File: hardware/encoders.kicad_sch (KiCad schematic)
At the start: 19 parts

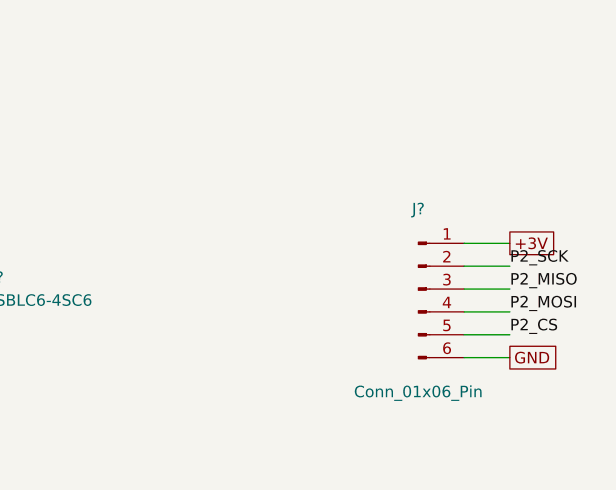
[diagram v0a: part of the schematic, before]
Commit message: Add sensing sheet; update MCU, CAN FD, encoder and root schematics
Co-Authored-By: Claude Opus 5.5 <noreply@anthropic.com>
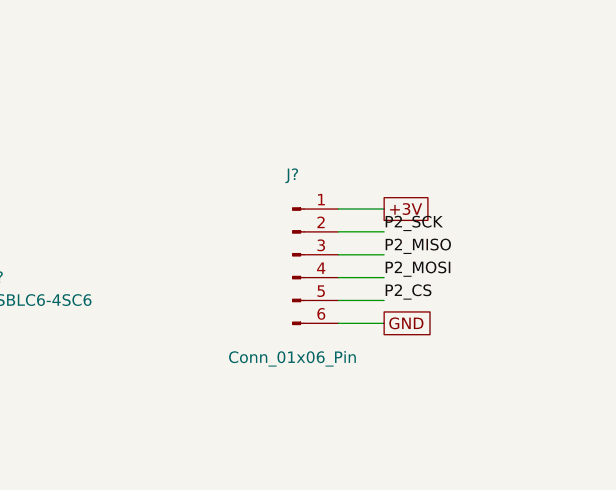
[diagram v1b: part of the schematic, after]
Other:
- moved on the sheet: J?

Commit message: Clean up schematic ERC; add project symbol library; update README
Fix dangling labels, floating pins and pin types across the sheets so
ERC reports 0 errors (see hardware/CHANGES.txt). Add PWR_FLAGs and move
TCAN1042GV, MA702GQ and the EMI filter to nexus_drive.kicad_sym.

Update the README layout, specs and schematic review status.

Co-Authored-By: Claude Opus 5.5 <noreply@anthropic.com>
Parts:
- U3, U4: renamed from U?; footprint (none) -> Package_TO_SOT_SMD:SOT-23-6
- U6: renamed from U?; symbol Sensor_Magnetic:MA702GQ -> nexus_drive:MA702GQ
- gave numbers to parts that had none: 16
